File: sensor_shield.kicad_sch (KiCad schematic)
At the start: 2 parts, among them J1 Conn_01x08, J2 Conn_01x06

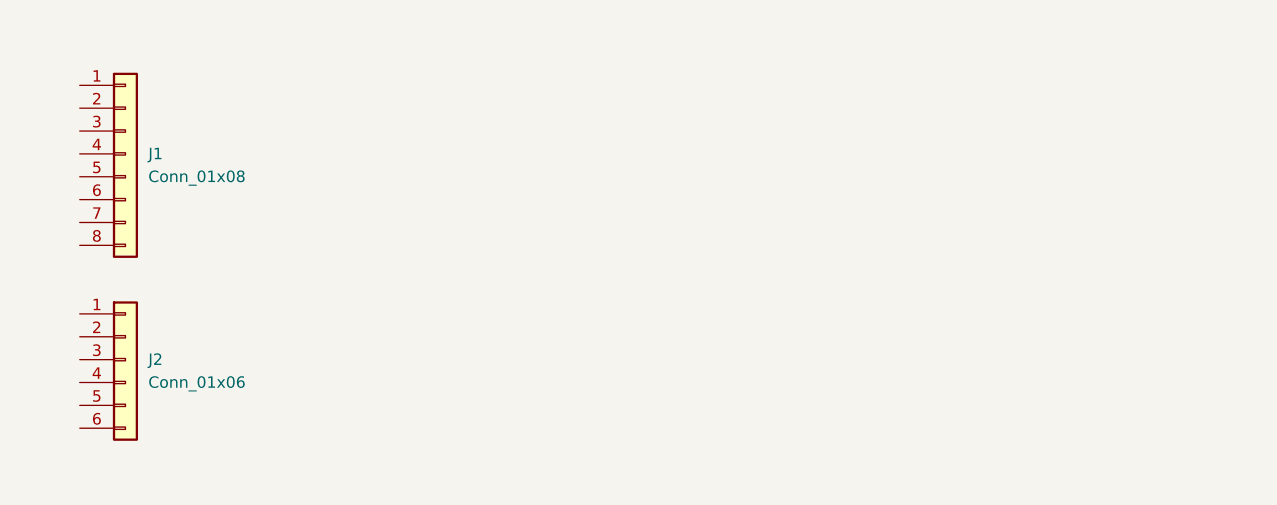
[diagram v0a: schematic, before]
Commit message: feat(basic): Add basic schematic with footprints
Signed-off-by: Vaishnav Sabari Girish <vaishnav.sabari.girish@gmail.com>
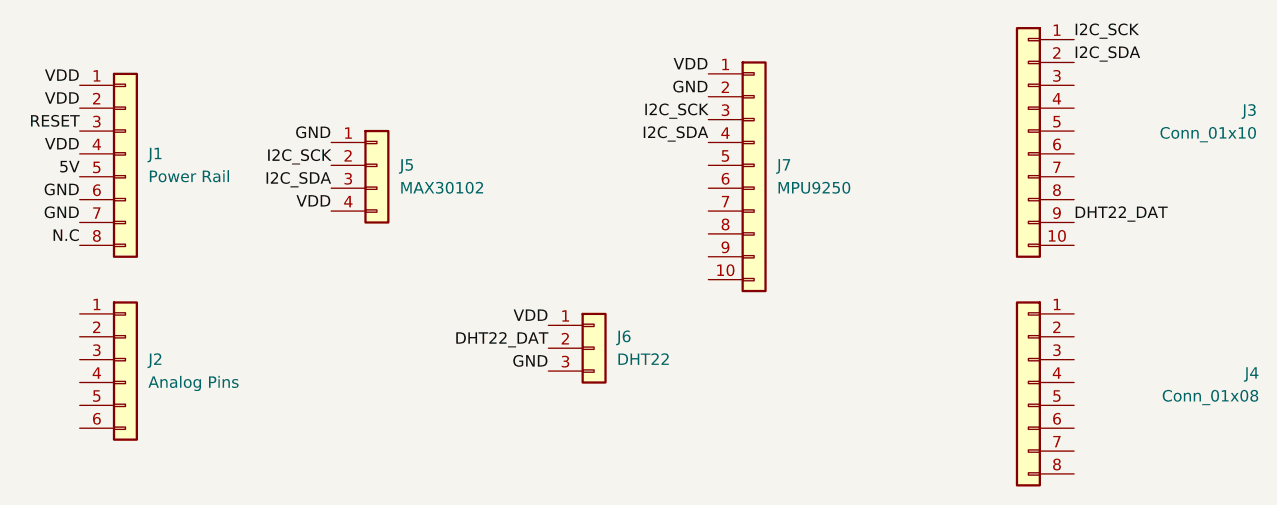
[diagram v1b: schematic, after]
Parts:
- added J3: Conn_01x10, Connector_PinHeader_2.54mm:PinHeader_1x10_P2.54mm_Vertical, symbol Connector_Generic:Conn_01x10
- added J4: Conn_01x08, Connector_PinHeader_2.54mm:PinHeader_1x08_P2.54mm_Vertical, symbol Connector_Generic:Conn_01x08
- added J5: MAX30102, Connector_PinHeader_2.54mm:PinHeader_1x04_P2.54mm_Vertical, symbol Connector_Generic:Conn_01x04
- added J6: DHT22, Connector_PinHeader_2.54mm:PinHeader_1x03_P2.54mm_Vertical, symbol Connector_Generic:Conn_01x03
- added J7: MPU9250, Connector_PinHeader_2.54mm:PinHeader_1x10_P2.54mm_Vertical, symbol Connector_Generic:Conn_01x10
- J1: value Conn_01x08 -> Power Rail; footprint (none) -> Connector_PinHeader_2.54mm:PinHeader_1x08_P2.54mm_Vertical
- J2: value Conn_01x06 -> Analog Pins; footprint (none) -> Connector_PinHeader_2.54mm:PinHeader_1x06_P2.54mm_Vertical
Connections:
- net VDD: now reaches J1.1 (Pin_1)
- net VDD: now also J1.2 (Pin_2), J1.4 (Pin_4), J5.4 (Pin_4), J6.1 (Pin_1), J7.1 (Pin_1)
- net RESET: now reaches J1.3 (Pin_3)
- net 5V: now reaches J1.5 (Pin_5)
- net GND: now reaches J1.6 (Pin_6)
- net GND: now also J1.7 (Pin_7), J5.1 (Pin_1), J6.3 (Pin_3), J7.2 (Pin_2)
- net N.C: now reaches J1.8 (Pin_8)
- new net DHT22_DAT: J3.9 (Pin_9), J6.2 (Pin_2)
- new net I2C_SCK: J3.1 (Pin_1), J5.2 (Pin_2), J7.3 (Pin_3)
- new net I2C_SDA: J3.2 (Pin_2), J5.3 (Pin_3), J7.4 (Pin_4)
